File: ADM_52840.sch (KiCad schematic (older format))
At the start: 33 parts, among them J1 JST, J2 SK6812_OUT, J3 Conn_01x15_Male, J4 Conn_01x19_Male, J5 JTAG, P1 USB_micro_B, Q1 DMP2045U, SW1 BTN1, SW2 BTN2, SW3 RESET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

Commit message: Seri + Corrections
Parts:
- J3: value Conn_01x15_Male -> Conn_01x16_Male; footprint Connector_PinSocket_2.54mm:PinSocket_1x15_P2.54mm_Vertical -> Connector_PinHeader_2.54mm:PinHeader_1x16_P2.54mm_Vertical; symbol Connector:Conn_01x15_Male -> Connector:Conn_01x16_Male
- J4: footprint Connector_PinSocket_2.54mm:PinSocket_1x18_P2.54mm_Vertical -> Connector_PinHeader_2.54mm:PinHeader_1x19_P2.54mm_Vertical; symbol Connector:Conn_01x18_Male -> Connector:Conn_01x19_Male
- J5: footprint Connector_PinSocket_2.54mm:PinSocket_2x03_P2.54mm_Vertical -> Connector_PinHeader_2.54mm:PinHeader_2x03_P2.54mm_Vertical
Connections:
- wire segments 259 -> 251
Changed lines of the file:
@@
 F 0 "J5" V 3375 7117 50  0000 C CNN
 F 1 "JTAG" V 3525 7025 50  0000 C CNN
-F 2 "Connector_PinSocket_2.54mm:PinSocket_2x03_P2.54mm_Vertical" H 3325 6700 50  0001 C CNN
+F 2 "Connector_PinHeader_2.54mm:PinHeader_2x03_P2.54mm_Vertical" H 3325 6700 50  0001 C CNN
 F 3 "~" H 3325 6700 50  0001 C CNN
 	1    3325 6700
@@
 	1    0    0    -1
 $EndComp
+Text GLabel 3500 7300 2    50   Input ~ 0
+SWDIO
 Text GLabel 3625 7100 2    50   Input ~ 0
-SWDIO
-Text GLabel 3500 7300 2    50   Input ~ 0
 SWDCLK
 Wire Wire Line
@@
 	1825 7150 1825 7300
 $Comp
-L Connector:Conn_01x15_Male J3
+L Connector:Conn_01x16_Male J3
 U 1 1 5FA23DAD
 P 7650 2300
 F 0 "J3" H 7775 1450 50  0000 R CNN
-F 1 "Conn_01x15_Male" H 7975 1275 50  0001 R CNN
-F 2 "Connector_PinSocket_2.54mm:PinSocket_1x15_P2.54mm_Vertical" H 7650 2300 50  0001 C CNN
+F 1 "Conn_01x16_Male" H 7975 1275 50  0001 R CNN
+F 2 "Connector_PinHeader_2.54mm:PinHeader_1x16_P2.54mm_Vertical" H 7650 2300 50  0001 C CNN
 F 3 "~" H 7650 2300 50  0001 C CNN
 	1    7650 2300
@@
 	6450 2300 6450 2275
 $Comp
-L Connector:Conn_01x18_Male J4
+L Connector:Conn_01x19_Male J4
 U 1 1 5FBCF5CF
 P 1750 4425
 F 0 "J4" V 1677 4353 50  0000 C CNN
 F 1 "Conn_01x19_Male" V 1586 4353 50  0001 C CNN
-F 2 "Connector_PinSocket_2.54mm:PinSocket_1x18_P2.54mm_Vertical" H 1750 4425 50  0001 C CNN
+F 2 "Connector_PinHeader_2.54mm:PinHeader_1x19_P2.54mm_Vertical" H 1750 4425 50  0001 C CNN
 F 3 "~" H 1750 4425 50  0001 C CNN
 	1    1750 4425
@@
 $EndComp
 Wire Wire Line
-	2550 3375 3525 3375
-Wire Wire Line
-	2450 3275 3525 3275
-Wire Wire Line
-	2350 3175 3525 3175
-Wire Wire Line
-	2250 3075 3525 3075
-Wire Wire Line
-	2150 2975 3525 2975
-Wire Wire Line
-	2050 2875 3525 2875
-Wire Wire Line
 	2475 1475 2475 1400
 Wire Wire Line
@@
 	550  1325 550  4025
 Wire Wire Line
-	1950 2775 1950 2975
-Wire Wire Line
-	1950 2775 3525 2775
-Wire Wire Line
-	1750 4225 1750 2975
-Wire Wire Line
-	1750 2975 1950 2975
-Wire Wire Line
-	1850 4225 1850 3075
-Wire Wire Line
-	1850 3075 2050 3075
-Wire Wire Line
-	2050 3075 2050 2875
-Wire Wire Line
-	1950 3150 2150 3150
-Wire Wire Line
-	1950 4225 1950 3150
-Wire Wire Line
-	2150 3150 2150 2975
-Wire Wire Line
-	2050 4225 2050 3250
-Wire Wire Line
-	2050 3250 2250 3250
-Wire Wire Line
-	2250 3250 2250 3075
-Wire Wire Line
-	2150 4225 2150 3325
-Wire Wire Line
-	2150 3325 2350 3325
-Wire Wire Line
-	2350 3325 2350 3175
-Wire Wire Line
-	2250 4225 2250 3425
-Wire Wire Line
-	2250 3425 2450 3425
-Wire Wire Line
-	2450 3425 2450 3275
-Wire Wire Line
-	2350 4225 2350 3550
-Wire Wire Line
-	2350 3550 2550 3550
-Wire Wire Line
-	2550 3550 2550 3375
-Wire Wire Line
 	4175 4550 3300 4550
 Wire Wire Line
-	3300 4550 3300 3650
-Wire Wire Line
-	3300 3650 2450 3650
-Wire Wire Line
-	2450 3650 2450 4225
+	3300 4550 3300 3500
+Wire Wire Line
+	3300 3500 2350 3500
+Wire Wire Line
+	2350 3500 2350 4225
 Wire Wire Line
 	4275 4675 3150 4675
 Wire Wire Line
-	3150 4675 3150 3750
-Wire Wire Line
-	3150 3750 2550 3750
-Wire Wire Line
-	2550 3750 2550 4225
+	3150 4675 3150 3600
+Wire Wire Line
+	3150 3600 2450 3600
+Wire Wire Line
+	2450 3600 2450 4225
 Wire Wire Line
 	4375 4800 3000 4800
 Wire Wire Line
-	3000 4800 3000 3850
-Wire Wire Line
-	3000 3850 2650 3850
-Wire Wire Line
-	2650 3850 2650 4225
+	3000 4800 3000 3700
+Wire Wire Line
+	3000 3700 2550 3700
+Wire Wire Line
+	2550 3700 2550 4225
 $Comp
 L Device:R R7
@@
 Connection ~ 1975 2475
 Wire Wire Line
-	3525 2675 1650 2675
-Wire Wire Line
-	1650 2675 1650 4225
+	3525 2675 1550 2675
+Wire Wire Line
+	1550 2675 1550 4225
 Wire Wire Line
 	3525 2575 2525 2575
@@
 	2525 2575 2525 2625
 Wire Wire Line
-	2525 2625 1550 2625
-Wire Wire Line
-	1550 2625 1550 4225
+	2525 2625 1450 2625
+Wire Wire Line
+	1450 2625 1450 4225
 Wire Wire Line
 	925  1875 925  2750
@@
 	875  1775 3525 1775
 Wire Wire Line
-	1050 3975 1050 4225
-Wire Wire Line
-	625  3975 1050 3975
-Wire Wire Line
-	950  4225 950  4025
-Wire Wire Line
-	550  4025 950  4025
-Wire Wire Line
-	700  3875 1150 3875
-Wire Wire Line
-	1150 3875 1150 4225
+	950  3975 950  4225
+Wire Wire Line
+	625  3975 950  3975
+Wire Wire Line
+	850  4225 850  4025
+Wire Wire Line
+	550  4025 850  4025
+Wire Wire Line
+	700  3875 1050 3875
+Wire Wire Line
+	1050 3875 1050 4225
 Wire Wire Line
 	700  1575 700  3875
 Wire Wire Line
-	775  3775 1250 3775
-Wire Wire Line
-	1250 3775 1250 4225
+	775  3775 1150 3775
+Wire Wire Line
+	1150 3775 1150 4225
 Wire Wire Line
 	775  1675 775  3775
@@
 	875  1775 875  3675
 Wire Wire Line
-	875  3675 1350 3675
-Wire Wire Line
-	1350 3675 1350 4225
-Wire Wire Line
-	1450 2750 1450 4225
-Wire Wire Line
-	925  2750 1450 2750
+	875  3675 1250 3675
+Wire Wire Line
+	1250 3675 1250 4225
+Wire Wire Line
+	1350 2750 1350 4225
+Wire Wire Line
+	925  2750 1350 2750
 Wire Wire Line
 	7375 3375 7375 3000
@@
 Wire Wire Line
 	1600 2075 1500 2075
+Wire Wire Line
+	7450 3100 7425 3100
+Wire Wire Line
+	7425 3100 7425 3525
+Wire Wire Line
+	7425 3525 7025 3525
+Text GLabel 7025 3525 0    50   Input ~ 0
+V_NRF
+Wire Wire Line
+	1650 2775 3525 2775
+Wire Wire Line
+	1650 2775 1650 4225
+Wire Wire Line
+	1750 2875 3525 2875
+Wire Wire Line
+	1750 2875 1750 4225
+Wire Wire Line
+	1850 2975 3525 2975
+Wire Wire Line
+	1850 2975 1850 4225
+Wire Wire Line
+	1950 3075 3525 3075
+Wire Wire Line
+	1950 3075 1950 4225
+Wire Wire Line
+	2050 3175 3525 3175
+Wire Wire Line
+	2050 3175 2050 4225
+Wire Wire Line
+	2150 3275 3525 3275
+Wire Wire Line
+	2150 3275 2150 4225
+Wire Wire Line
+	2250 3375 3525 3375
+Wire Wire Line
+	2250 3375 2250 4225
+Wire Wire Line
+	2650 4225 2650 3900
+Wire Wire Line
+	2650 3900 2825 3900
+Wire Wire Line
+	2825 3900 2825 4275
+$Comp
+L power:GND #PWR0104
+U 1 1 5FE7406E
+P 2825 4275
+F 0 "#PWR0104" H 2825 4025 50  0001 C CNN
+F 1 "GND" H 2830 4102 50  0000 C CNN
+F 2 "" H 2825 4275 50  0001 C CNN
+F 3 "" H 2825 4275 50  0001 C CNN
+	1    2825 4275
+	1    0    0    -1
+$EndComp
 $EndSCHEMATC

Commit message: Add some capa
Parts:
- added C? (x4): 100nF, symbol Device:C
- added C?: 10uF, symbol Device:C
- added C?: 100uF, symbol Device:C
- added R? (x3): 10k mini, symbol Device:R
- added R? (x2): 33R, symbol Device:R
- U2: symbol Memory_Flash:MX25R3235FZNxx1 -> ADM_52840-rescue:MX25R3235FZNxx1-Memory_Flash
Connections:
- net labels added: P0.32, P0.33
- wire segments 251 -> 274
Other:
- moved on the sheet: D5, J2, P1, SW1, SW2

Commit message: route
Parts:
- removed R? (x2): 33R, symbol Device:R
- C10, C11, C8, C9: renamed from C?; footprint (none) -> LEGACY:SM0603
- C12: renamed from C?; value 100uF -> 10uF; footprint (none) -> LEGACY:SM0805
- C7: renamed from C?; footprint (none) -> LEGACY:SM0805
- J2: footprint LEGACY:pin_array_3x1 -> Connector_PinHeader_2.54mm:PinHeader_1x03_P2.54mm_Vertical
- R10, R11, R9: renamed from R?; footprint (none) -> LEGACY:SM0603
- U2: symbol ADM_52840-rescue:MX25R3235FZNxx1-Memory_Flash -> Memory_Flash:MX25R3235FZNxx1
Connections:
- wire segments 274 -> 273
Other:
- note added: "Back"
- note added: "Button 1"
- note added: "Button 2"
- note added: "Front"
- moved on the sheet: C10, C2, C8, C9, D1, D2, J3, J4, R10, R11, R7, R8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

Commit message: Done?
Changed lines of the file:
@@
 	3650 5000 7975 5000
 $Comp
-L seri:LOGO #G1
+L ADM_52840-rescue:LOGO-seri #G1
 U 1 1 5FA34F44
 P 8550 6825
@@
 $EndComp
 $Comp
-L seri:LOGO #G2
+L ADM_52840-rescue:LOGO-seri #G2
 U 1 1 5FA358D5
 P 9600 6825

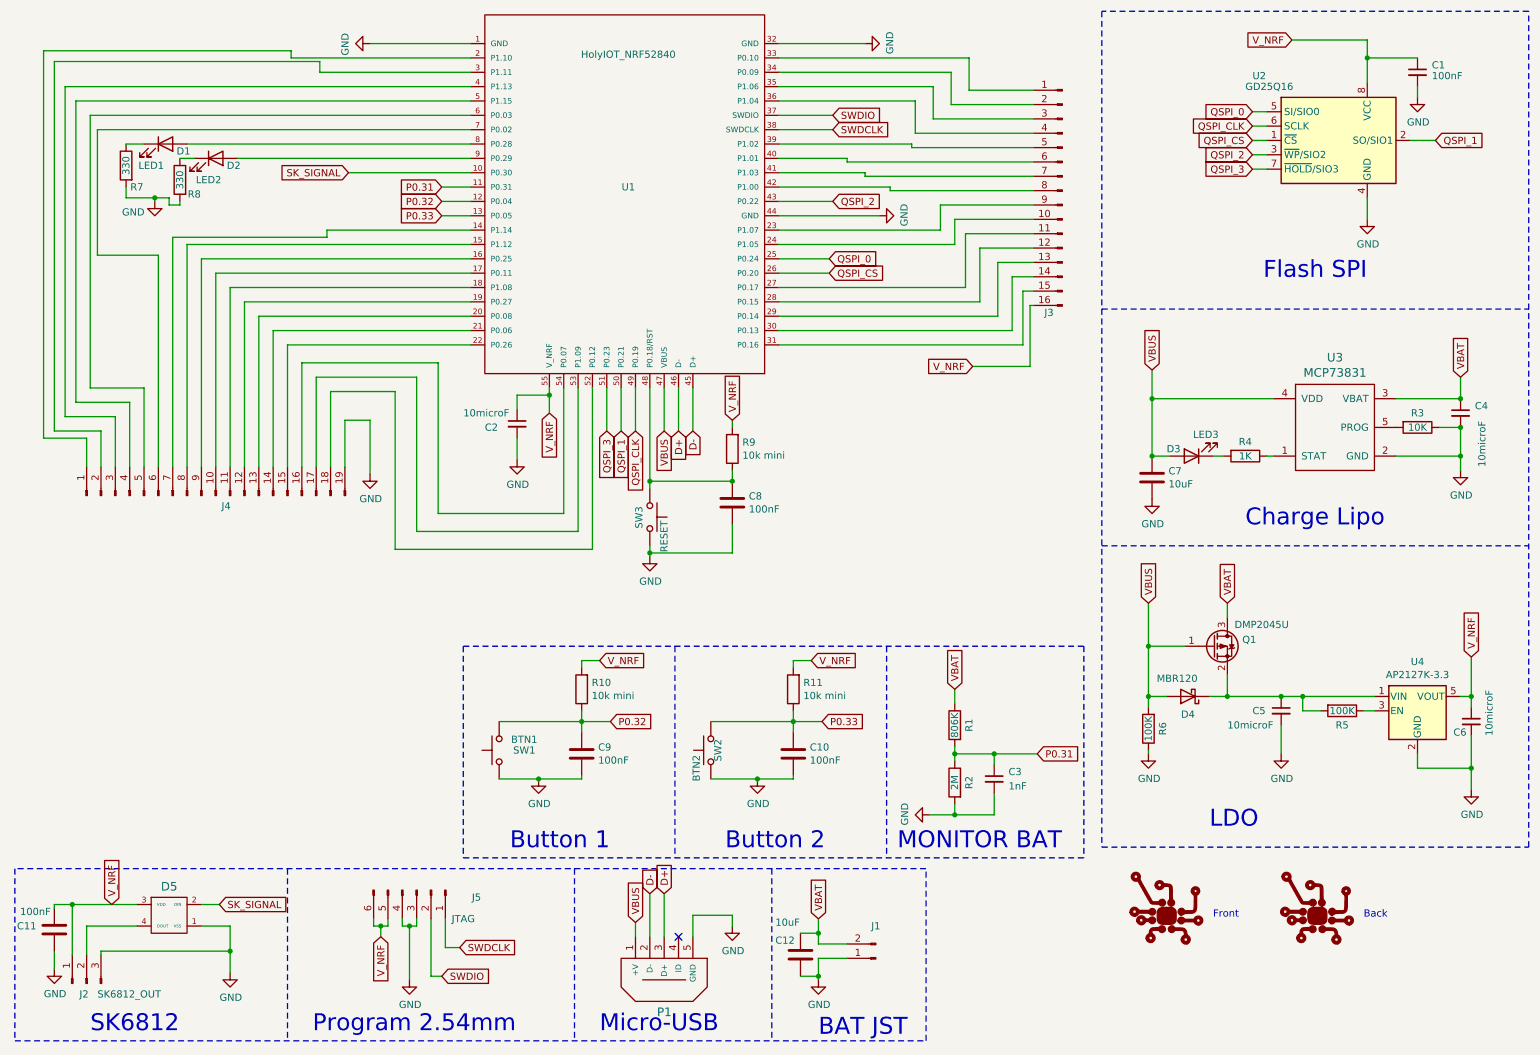
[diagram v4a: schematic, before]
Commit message: Pinout SPi
Rework pinout SPI + SK6812 + Footprint SPI
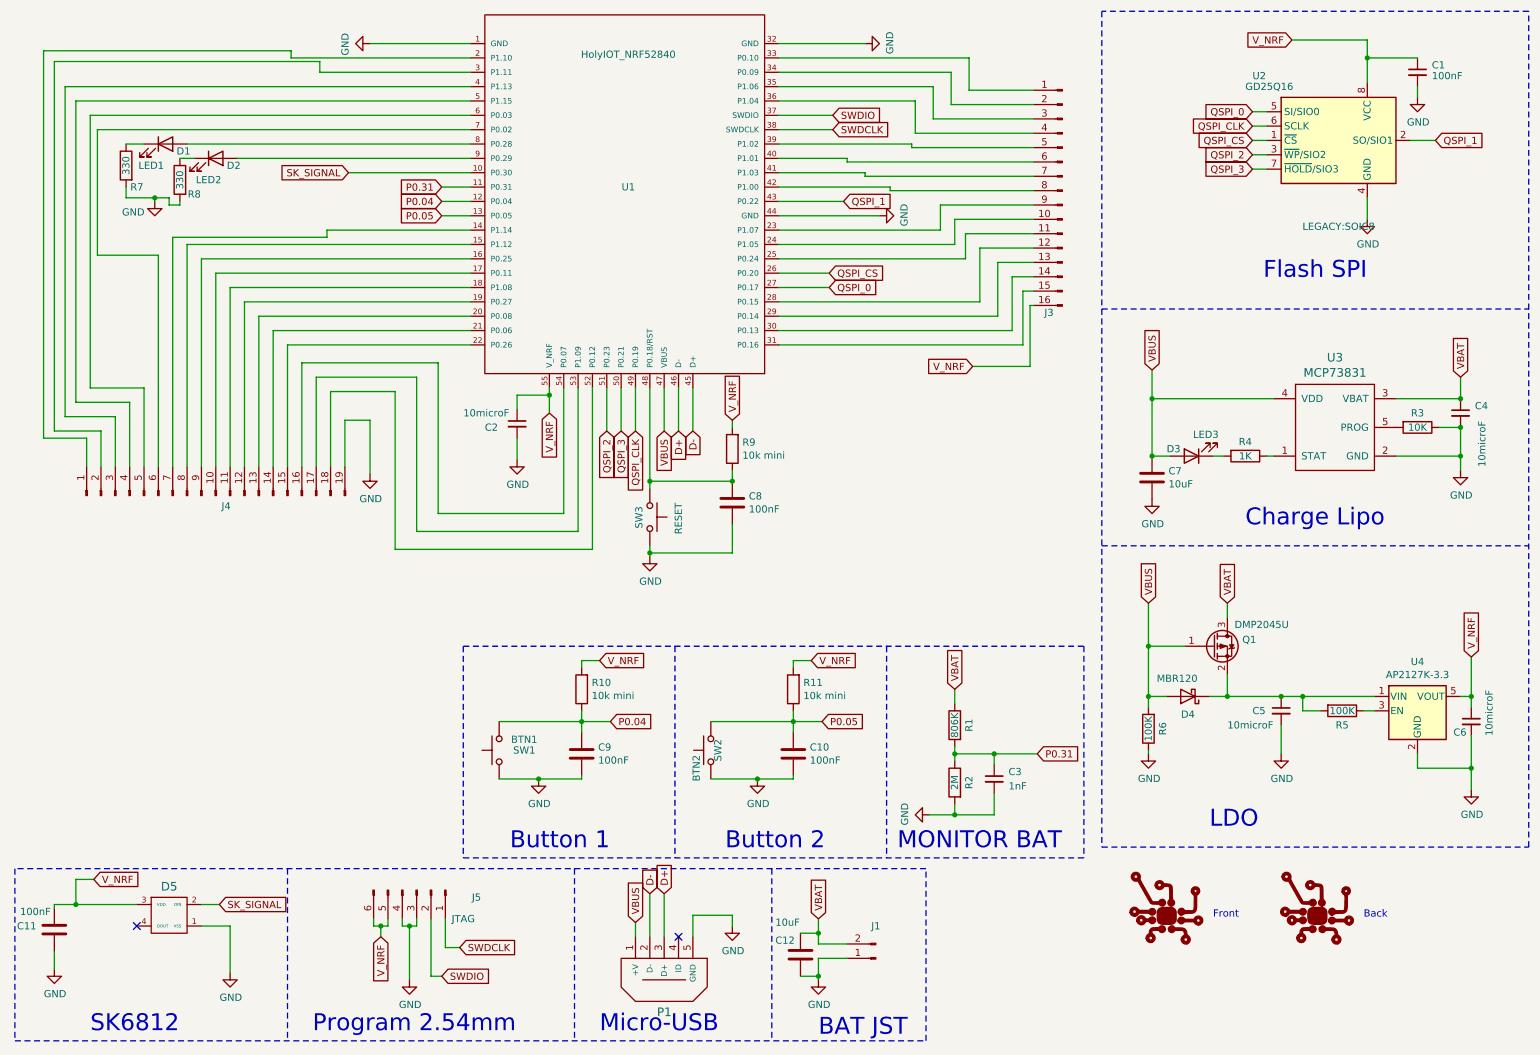
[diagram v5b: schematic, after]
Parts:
- removed J2: SK6812_OUT, Connector_PinHeader_2.54mm:PinHeader_1x03_P2.54mm_Vertical, symbol Connector:Conn_01x03_Male
- U2: footprint LEGACY:SON80P400X300X60-10N -> LEGACY:SOIC8
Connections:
- net QSPI_0: now also U1.27 (P0.17); no longer U1.25 (P0.24)
- net QSPI_1: now also U1.43 (P0.22); no longer U1.50 (P0.21)
- net QSPI_2: now also U1.51 (P0.23); no longer U1.43 (P0.22)
- net QSPI_3: now also U1.50 (P0.21); no longer U1.51 (P0.23)
- net at J3.11 (Pin_11): now also U1.25 (P0.24); no longer U1.27 (P0.17)
- net P0.32 renamed P0.04
- net P0.33 renamed P0.05
- no-connect marks 1 -> 2
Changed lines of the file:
@@
 P 4950 4100
 F 0 "SW3" H 4875 4025 50  0000 L CNN
-F 1 "RESET" H 4975 4200 50  0000 L CNN
+F 1 "RESET" H 4850 4300 50  0000 L CNN
 F 2 "LEGACY:SWITCH_CMS" H 4950 4300 50  0001 C CNN
 F 3 "~" H 4950 4300 50  0001 C CNN
@@
 F 0 "U2" H 9150 1925 50  0000 L CNN
 F 1 "GD25Q16" H 9100 1850 50  0000 L CNN
-F 2 "LEGACY:SON80P400X300X60-10N" H 9750 875 50  0001 C CNN
+F 2 "LEGACY:SOIC8" H 9750 875 50  0000 C CNN
 F 3 "" H 9750 1475 50  0001 C CNN
 	1    9750 1475
@@
 Text GLabel 9150 1475 0    50   Input ~ 0
 QSPI_CS
-Text GLabel 6200 2300 2    50   Input ~ 0
+Text GLabel 6200 2500 2    50   Input ~ 0
 QSPI_0
-Text GLabel 6225 1900 2    50   Input ~ 0
+Text GLabel 4650 3500 3    50   Input ~ 0
 QSPI_2
-Text GLabel 4650 3500 3    50   Input ~ 0
+Text GLabel 4750 3500 3    50   Input ~ 0
 QSPI_3
 Text GLabel 4850 3500 3    50   Input ~ 0
@@
 Wire Wire Line
 	1825 6950 2025 6950
-Wire Wire Line
-	2025 6950 2025 7125
-Text GLabel 1200 6800 1    50   Input ~ 0
+Text GLabel 1075 6625 2    50   Input ~ 0
 V_NRF
 $Comp
@@
 Wire Wire Line
 	1950 6800 1825 6800
-$Comp
-L Connector:Conn_01x03_Male J2
-U 1 1 617280D9
-P 1025 7350
-F 0 "J2" V 950 7400 50  0000 R CNN
-F 1 "SK6812_OUT" V 950 7275 50  0000 R CNN
-F 2 "Connector_PinHeader_2.54mm:PinHeader_1x03_P2.54mm_Vertical" H 1025 7350 50  0001 C CNN
-F 3 "~" H 1025 7350 50  0001 C CNN
-	1    1025 7350
-	0    -1   -1   0
-$EndComp
-Wire Wire Line
-	1375 6950 1025 6950
-Wire Wire Line
-	1025 6950 1025 7150
 Text GLabel 6200 2400 2    50   Input ~ 0
 QSPI_CS
-Text GLabel 4750 3500 3    50   Input ~ 0
+Text GLabel 6300 1900 2    50   Input ~ 0
 QSPI_1
 Connection ~ 7075 6175
@@
 	5850 2400 6200 2400
 Wire Wire Line
-	5850 2300 6200 2300
-Wire Wire Line
 	5850 2000 6550 2000
 Wire Wire Line
-	5850 1900 6225 1900
-Wire Wire Line
 	5850 800  6450 800
-Wire Wire Line
-	925  6800 1375 6800
-Wire Wire Line
-	1125 7150 1125 7125
-Wire Wire Line
-	1125 7125 2025 7125
-Connection ~ 2025 7125
-Wire Wire Line
-	2025 7125 2025 7275
 $Comp
 L Connector:Conn_01x16_Male J3
@@
 	5850 2200 7075 2200
 Wire Wire Line
-	7150 2500 7150 2125
-Wire Wire Line
 	7150 2125 7625 2125
-Wire Wire Line
-	5850 2500 7150 2500
 Wire Wire Line
 	7250 2600 7250 2225
@@
 	4950 3850 5525 3850
 Text GLabel 3500 1900 0    50   Input ~ 0
-P0.32
+P0.04
 Text GLabel 3500 2000 0    50   Input ~ 0
-P0.33
+P0.05
 Wire Wire Line
 	3700 1900 3500 1900
@@
 	3500 2000 3700 2000
 Text GLabel 4675 5525 2    50   Input ~ 0
-P0.32
+P0.04
 Text GLabel 6150 5525 2    50   Input ~ 0
-P0.33
+P0.05
 $Comp
 L Device:R R10
@@
 $EndComp
 Wire Wire Line
-	925  6800 925  7150
-Wire Wire Line
-	925  6800 800  6800
-Wire Wire Line
 	800  6800 800  6825
-Connection ~ 925  6800
 $Comp
 L power:GND #PWR0108
@@
 Wire Wire Line
 	4950 6725 4950 7025
+Wire Wire Line
+	5850 2300 7150 2300
+Wire Wire Line
+	7150 2300 7150 2125
+Wire Wire Line
+	5850 2500 6200 2500
+Wire Wire Line
+	5850 1900 6300 1900
+NoConn ~ 1375 6950
+Wire Wire Line
+	800  6800 950  6800
+Wire Wire Line
+	1075 6625 950  6625
+Wire Wire Line
+	950  6625 950  6800
+Connection ~ 950  6800
+Wire Wire Line
+	950  6800 1375 6800
+Wire Wire Line
+	2025 6950 2025 7275
 $EndSCHEMATC
